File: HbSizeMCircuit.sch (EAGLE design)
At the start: 24 parts

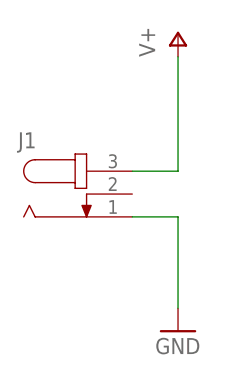
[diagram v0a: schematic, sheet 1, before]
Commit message: DCジャックを変更
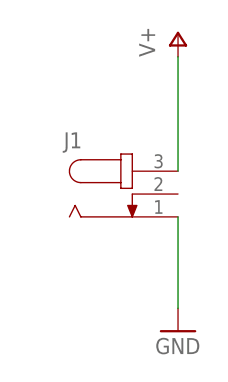
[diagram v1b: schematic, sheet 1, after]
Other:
- moved on the sheet: J1
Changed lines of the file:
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@@
 <part name="P+6" library="supply1" library_urn="urn:adsk.eagle:library:371" deviceset="+5V" device=""/>
 <part name="GND7" library="supply1" library_urn="urn:adsk.eagle:library:371" deviceset="GND" device=""/>
-<part name="J1" library="HbSizeM" deviceset="JACK-PLUG" device="1"/>
 <part name="U$7" library="HbSizeM" deviceset="NN_SERVO" device=""/>
 <part name="U$11" library="HbSizeM" deviceset="NN_SERVO" device=""/>
@@
 <part name="U$10" library="HbSizeM" deviceset="NN_SENSOR" device=""/>
 <part name="U$16" library="HbHandBoard_SizeS" deviceset="53398-0371" device=""/>
+<part name="J1" library="HbSizeM" deviceset="JACK-PLUG" device="1"/>
 </parts>
 <sheets>
@@
 <instance part="P+1" gate="1" x="76.2" y="231.14"/>
 <instance part="GND1" gate="1" x="76.2" y="198.12"/>
-<instance part="J1" gate="G$1" x="66.04" y="213.36"/>
+<instance part="J1" gate="G$1" x="71.12" y="213.36"/>
 </instances>
 <busses>
@@
 <segment>
 <pinref part="P+1" gate="1" pin="V+"/>
-<wire x1="71.12" y1="215.9" x2="76.2" y2="215.9" width="0.1524" layer="91"/>
 <wire x1="76.2" y1="215.9" x2="76.2" y2="228.6" width="0.1524" layer="91"/>
 <pinref part="J1" gate="G$1" pin="3"/>
@@
 <wire x1="76.2" y1="210.82" x2="76.2" y2="200.66" width="0.1524" layer="91"/>
 <pinref part="J1" gate="G$1" pin="1"/>
-<wire x1="76.2" y1="210.82" x2="71.12" y2="210.82" width="0.1524" layer="91"/>
 </segment>
 </net>
